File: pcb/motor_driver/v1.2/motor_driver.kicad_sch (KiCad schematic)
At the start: 5 parts, among them J1 XT60PW-M

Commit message: perf: fix pcb for v1.2
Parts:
- removed J1: XT60PW-M, Connector_AMASS:AMASS_XT60-M_1x02_P7.20mm_Vertical, symbol bldc_lib:XT60PW-M
- added J1: XT30, Connector_AMASS:AMASS_XT30U-F_1x02_P5.0mm_Vertical, symbol Connector_Generic:Conn_01x02
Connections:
- net +BATT: now also J1.2 (Pin_2)
- net GND: now also J1.1 (Pin_1)
- no-connect marks 2 -> 0
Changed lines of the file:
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@@
 		(color 0 0 0 0)
-	)
-	(no_connect
-		(at 96.52 80.01)
-	)
-	(no_connect
-		(at 96.52 82.55)
 	)
 	(wire
@@
 	)
 	(symbol
+		(lib_id "Connector_Generic:Conn_01x02")
+		(at 81.28 80.01 0)
+		(unit 1)
+		(exclude_from_sim no)
+		(in_bom yes)
+		(on_board yes)
+		(dnp no)
+		(fields_autoplaced yes)
+		(property "Reference" "J1"
+			(at 83.82 80.0099 0)
+			(effects
+				(font
+					(size 1.27 1.27)
+				)
+				(justify left)
+			)
+		)
+		(property "Value" "XT30"
+			(at 83.82 82.5499 0)
+			(effects
+				(font
+					(size 1.27 1.27)
+				)
+				(justify left)
+			)
+		)
+		(property "Footprint" "Connector_AMASS:AMASS_XT30U-F_1x02_P5.0mm_Vertical"
+			(at 81.28 80.01 0)
+			(effects
+				(font
+					(size 1.27 1.27)
+				)
+				(hide yes)
+			)
+		)
+		(property "Datasheet" "~"
+			(at 81.28 80.01 0)
+			(effects
+				(font
+					(size 1.27 1.27)
+				)
+				(hide yes)
+			)
+		)
+		(property "Description" "Generic connector, single row, 01x02, script generated (kicad-library-utils/schlib/autogen/connector/)"
+			(at 81.28 80.01 0)
+			(effects
+				(font
+					(size 1.27 1.27)
+				)
+				(hide yes)
+			)
+		)
+		(pin "2"
+		)
+		(pin "1"
+		)
+		(instances
+			(project ""
+				(path "/1ef6600e-ea1d-4a9a-8ae5-1c3f7136836c"
+					(reference "J1")
+					(unit 1)
+				)
+			)
+		)
+	)
+	(symbol
 		(lib_id "Mechanical:MountingHole")
 		(at 71.12 127 0)
@@
 					(unit 1)
 				)
-			)
-		)
-	)
-	(symbol
-		(lib_id "bldc_lib:XT60PW-M")
-		(at 87.63 74.93 0)
-		(unit 1)
-		(exclude_from_sim no)
-		(in_bom yes)
-		(on_board yes)
-		(dnp no)
-		(fields_autoplaced yes)
-		(property "Reference" "J1"
-			(at 86.36 72.39 0)
-			(effects
-				(font
-					(size 1.27 1.27)
-				)
-			)
-		)
-		(property "Value" "XT60PW-M"
-			(at 86.36 74.93 0)
-			(effects
-				(font
-					(size 1.27 1.27)
-				)
-			)
-		)
-		(property "Footprint" "Connector_AMASS:AMASS_XT60-M_1x02_P7.20mm_Vertical"
-			(at 76.2 80.01 0)
-			(effects
-				(font
-					(size 1.27 1.27)
-				)
-				(hide yes)
-			)
-		)
-		(property "Datasheet" ""
-			(at 76.2 80.01 0)
-			(effects
-				(font
-					(size 1.27 1.27)
-				)
-				(hide yes)
-			)
-		)
-		(property "Description" ""
-			(at 87.63 74.93 0)
-			(effects
-				(font
-					(size 1.27 1.27)
-				)
-				(hide yes)
-			)
-		)
-		(property "Reference_1" "J"
-			(at 104.14 67.31 0)
-			(effects
-				(font
-					(size 1.27 1.27)
-				)
-				(justify left top)
-				(hide yes)
-			)
-		)
-		(property "Value_1" "XT60PW-M"
-			(at 104.14 69.85 0)
-			(effects
-				(font
-					(size 1.27 1.27)
-				)
-				(justify left top)
-				(hide yes)
-			)
-		)
-		(property "Footprint_1" "XT60PWM"
-			(at 104.14 169.85 0)
-			(effects
-				(font
-					(size 1.27 1.27)
-				)
-				(justify left top)
-				(hide yes)
-			)
-		)
-		(property "Datasheet_1" "https://www.tme.eu/Document/9b8d0c5eb7094295f3d3112c214d3ade/XT60PW%20SPEC.pdf"
-			(at 104.14 269.85 0)
-			(effects
-				(font
-					(size 1.27 1.27)
-				)
-				(justify left top)
-				(hide yes)
-			)
-		)
-		(property "Height" "8.4"
-			(at 104.14 469.85 0)
-			(effects
-				(font
-					(size 1.27 1.27)
-				)
-				(justify left top)
-				(hide yes)
-			)
-		)
-		(property "Manufacturer_Name" "Changzou Amass Elec"
-			(at 104.14 569.85 0)
-			(effects
-				(font
-					(size 1.27 1.27)
-				)
-				(justify left top)
-				(hide yes)
-			)
-		)
-		(property "Manufacturer_Part_Number" "XT60PW-M"
-			(at 104.14 669.85 0)
-			(effects
-				(font
-					(size 1.27 1.27)
-				)
-				(justify left top)
-				(hide yes)
-			)
-		)
-		(property "Mouser Part Number" ""
-			(at 104.14 769.85 0)
-			(effects
-				(font
-					(size 1.27 1.27)
-				)
-				(justify left top)
-				(hide yes)
-			)
-		)
-		(property "Mouser Price/Stock" ""
-			(at 104.14 869.85 0)
-			(effects
-				(font
-					(size 1.27 1.27)
-				)
-				(justify left top)
-				(hide yes)
-			)
-		)
-		(property "Arrow Part Number" ""
-			(at 104.14 969.85 0)
-			(effects
-				(font
-					(size 1.27 1.27)
-				)
-				(justify left top)
-				(hide yes)
-			)
-		)
-		(property "Arrow Price/Stock" ""
-			(at 104.14 1069.85 0)
-			(effects
-				(font
-					(size 1.27 1.27)
-				)
-				(justify left top)
-				(hide yes)
-			)
-		)
-		(pin "1"
-		)
-		(pin "2"
-		)
-		(pin "3"
-		)
-		(pin "4"
-		)
-		(instances
-			(project "motor_driver"
-				(path "/1ef6600e-ea1d-4a9a-8ae5-1c3f7136836c"
-					(reference "J1")
-					(unit 1)
-				)

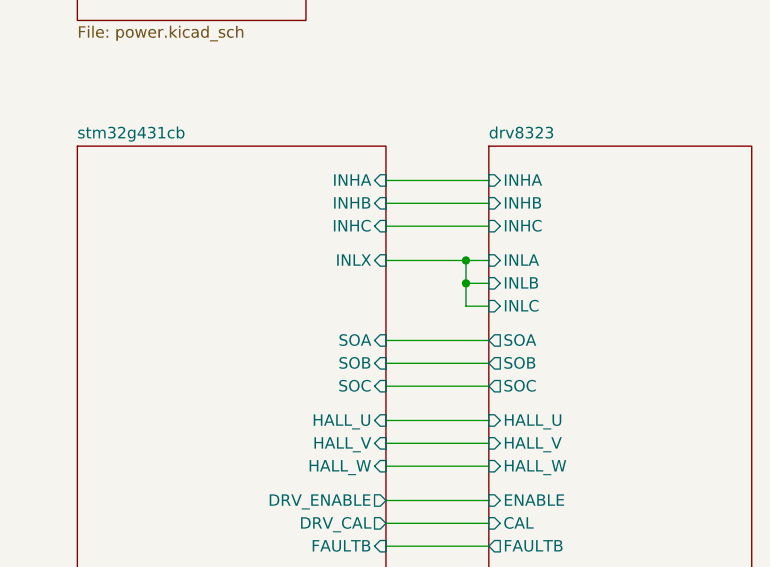
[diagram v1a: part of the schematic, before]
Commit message: perf: update motor driver pdb
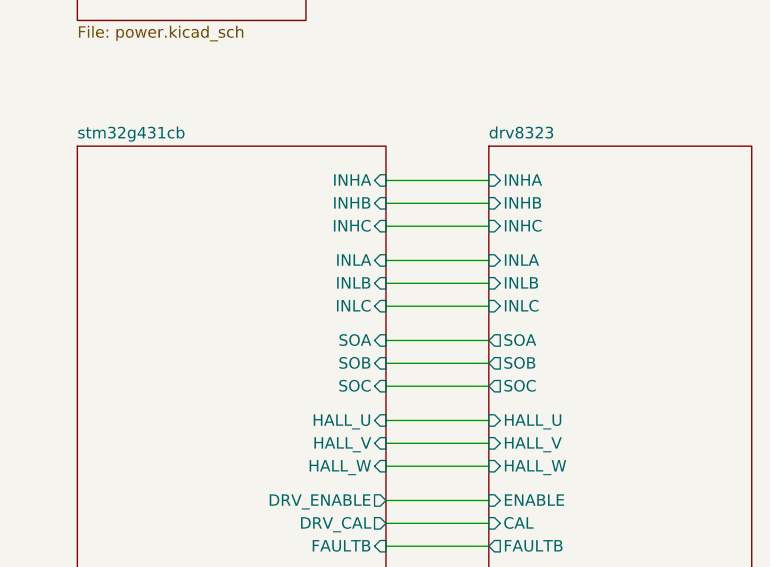
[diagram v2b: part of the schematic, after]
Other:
- sheet stm32g431cb ports: added INLA, INLB, INLC; removed INLX
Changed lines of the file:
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@@
 	(generator_version "8.0")
 	(paper "A4")
-	(junction
-		(at 156.21 82.55)
-		(diameter 0)
-		(color 0 0 0 0)
-	)
-	(junction
-		(at 156.21 85.09)
-		(diameter 0)
-		(color 0 0 0 0)
-	)
-	(wire
-		(pts
-			(xy 156.21 87.63) (xy 156.21 85.09)
-		)
-		(stroke
-			(width 0)
-			(type default)
-		)
-	)
 	(wire
 		(pts
@@
 	(wire
 		(pts
-			(xy 147.32 82.55) (xy 156.21 82.55)
+			(xy 147.32 82.55) (xy 158.75 82.55)
 		)
 		(stroke
@@
 	(wire
 		(pts
-			(xy 156.21 82.55) (xy 158.75 82.55)
-		)
-		(stroke
-			(width 0)
-			(type default)
-		)
-	)
-	(wire
-		(pts
 			(xy 147.32 119.38) (xy 158.75 119.38)
 		)
@@
 	(wire
 		(pts
-			(xy 158.75 87.63) (xy 156.21 87.63)
-		)
-		(stroke
-			(width 0)
-			(type default)
-		)
-	)
-	(wire
-		(pts
 			(xy 76.2 80.01) (xy 72.39 80.01)
 		)
@@
 	(wire
 		(pts
+			(xy 147.32 85.09) (xy 158.75 85.09)
+		)
+		(stroke
+			(width 0)
+			(type default)
+		)
+	)
+	(wire
+		(pts
 			(xy 147.32 135.89) (xy 158.75 135.89)
 		)
@@
 	(wire
 		(pts
+			(xy 147.32 87.63) (xy 158.75 87.63)
+		)
+		(stroke
+			(width 0)
+			(type default)
+		)
+	)
+	(wire
+		(pts
 			(xy 147.32 105.41) (xy 158.75 105.41)
 		)
@@
 		(pts
 			(xy 147.32 78.74) (xy 158.75 78.74)
-		)
-		(stroke
-			(width 0)
-			(type default)
-		)
-	)
-	(wire
-		(pts
-			(xy 158.75 85.09) (xy 156.21 85.09)
-		)
-		(stroke
-			(width 0)
-			(type default)
-		)
-	)
-	(wire
-		(pts
-			(xy 156.21 85.09) (xy 156.21 82.55)
 		)
 		(stroke
@@
 			)
 		)
-		(pin "INLX" input
-			(at 147.32 82.55 0)
-			(effects
-				(font
-					(size 1.27 1.27)
-				)
-				(justify right)
-			)
-		)
 		(pin "INHC" input
 			(at 147.32 78.74 0)
@@
 			(effects
 				(font
+					(size 1.27 1.27)
+				)
+				(justify right)
+			)
+		)
+		(pin "INLB" input
+			(at 147.32 85.09 0)
+			(effects
+				(font
+					(size 1.27 1.27)
+				)
+				(justify right)
+			)
+		)
+		(pin "INLA" input
+			(at 147.32 82.55 0)
+			(effects
+				(font
+					(size 1.27 1.27)
+				)
+				(justify right)
+			)
+		)
+		(pin "INLC" input
+			(at 147.32 87.63 0)
+			(effects
+				(font
